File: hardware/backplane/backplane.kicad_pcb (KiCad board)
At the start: 2 copper layers, 200 x 124 mm, 12 parts, among them J1 C96ABC, J2 C96ABC, J3 C96ABC, J4 C96ABC, J5 C96ABC, J6 C96ABC, J7 C96ABC, J8 C96ABC

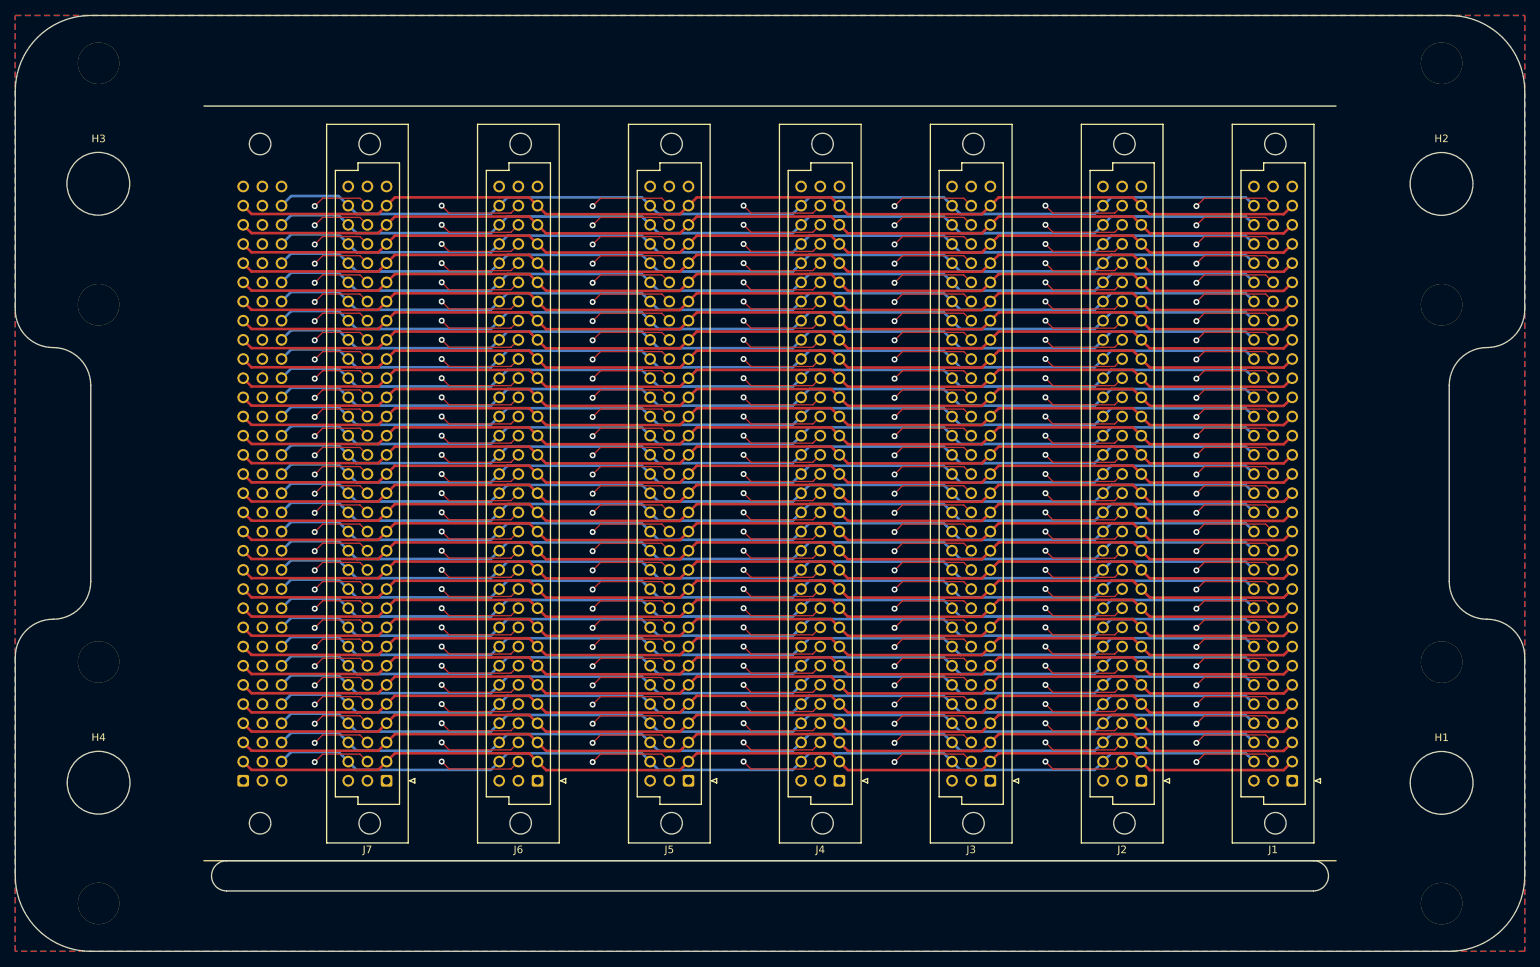
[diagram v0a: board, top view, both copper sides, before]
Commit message: backplane: fix spacing to use 5.08mm HP, expand to 8 back slots with 3/4 spacing
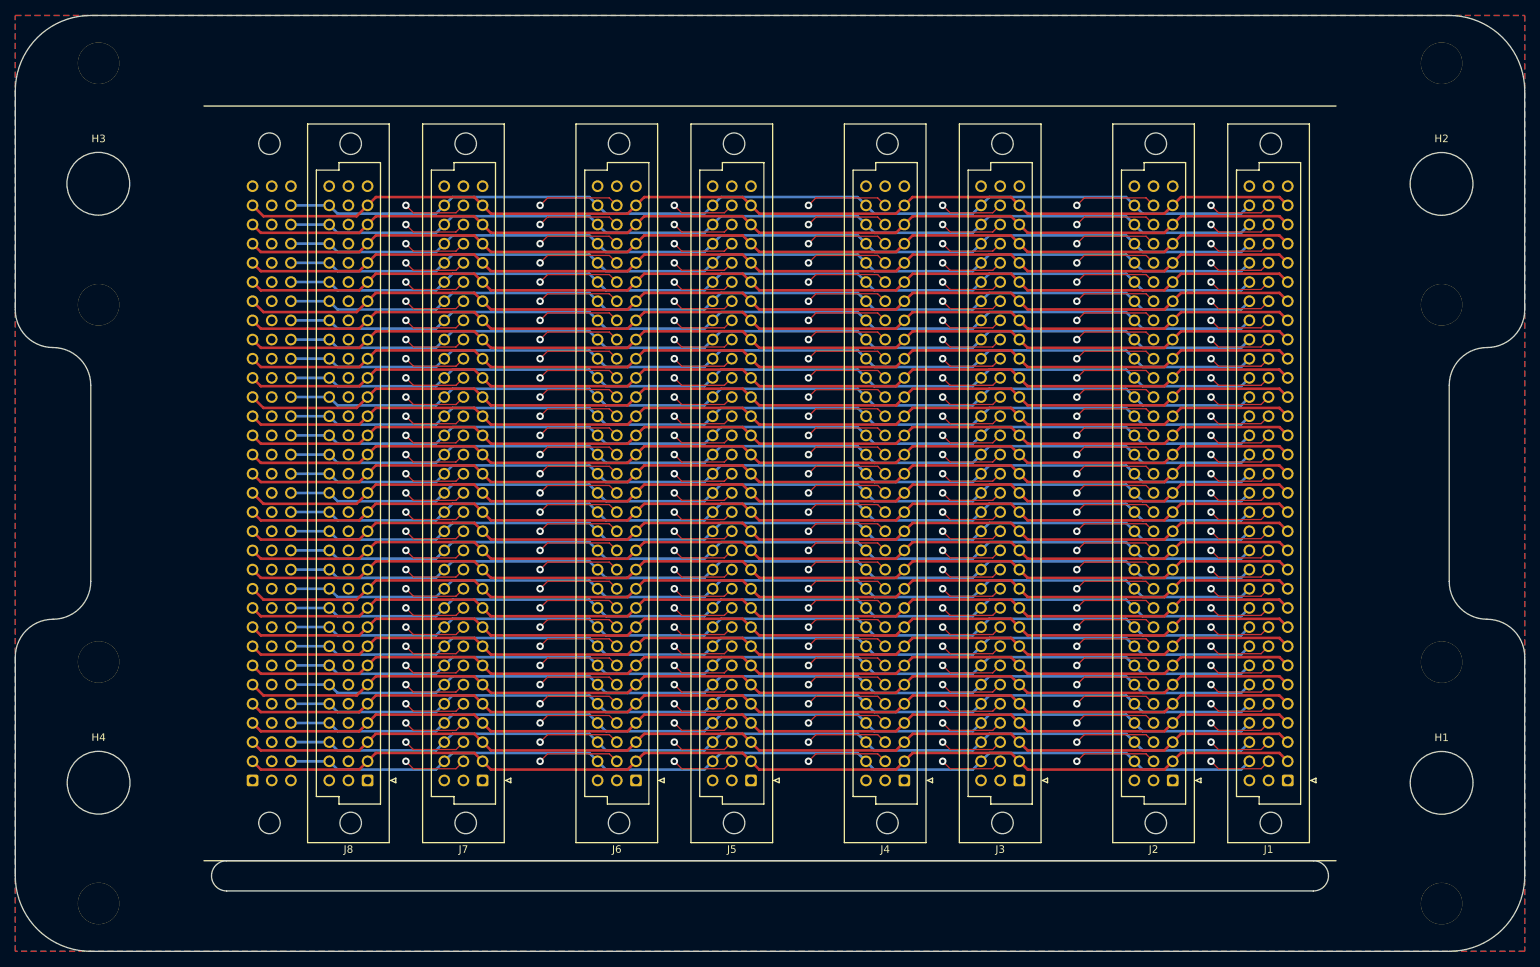
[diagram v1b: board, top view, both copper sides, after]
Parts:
- added J9: C96ABC, Connector_DIN:DIN41612_C_3x32_Female_Vertical_THT, B.Cu at (75.5, 129.9)
- J8: moved to F.Cu
- moved J8 16.5 mm to (90.8, 129.9), turned to 180 degrees
- moved J6 13.0 mm to (126.3, 129.9)
- moved J7 12.7 mm to (106.0, 129.9)
- moved J4 8.60 mm to (161.9, 129.9)
- moved J5 8.28 mm to (141.6, 129.9)
- moved J2 4.16 mm to (197.4, 129.9)
- moved J3 3.84 mm to (177.1, 129.9)
- moved J1 0.60 mm to (212.7, 129.9)
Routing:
- net B2J1: track 11.0 -> 8.44 mm
- net B7J1: track 11.0 -> 8.44 mm
- net B2J5: track 11.0 -> 8.44 mm
- net B28J1: track 11.0 -> 8.44 mm
- net B2J3: track 11.0 -> 8.44 mm
- net B9J1: track 11.0 -> 8.44 mm
- net B8J1: track 11.0 -> 8.44 mm
- net B6J1: track 11.0 -> 8.44 mm
- net B4J1: track 11.0 -> 8.44 mm
- net B29J1: track 11.0 -> 8.44 mm
- net B25J1: track 11.0 -> 8.44 mm
- net B24J1: track 11.0 -> 8.44 mm
- net B22J1: track 11.0 -> 8.44 mm
- net B20J1: track 11.0 -> 8.44 mm
- net B18J1: track 11.0 -> 8.44 mm
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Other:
- net class B: via_dia 1.5 -> 1; via_drill 0.6 -> 0.5

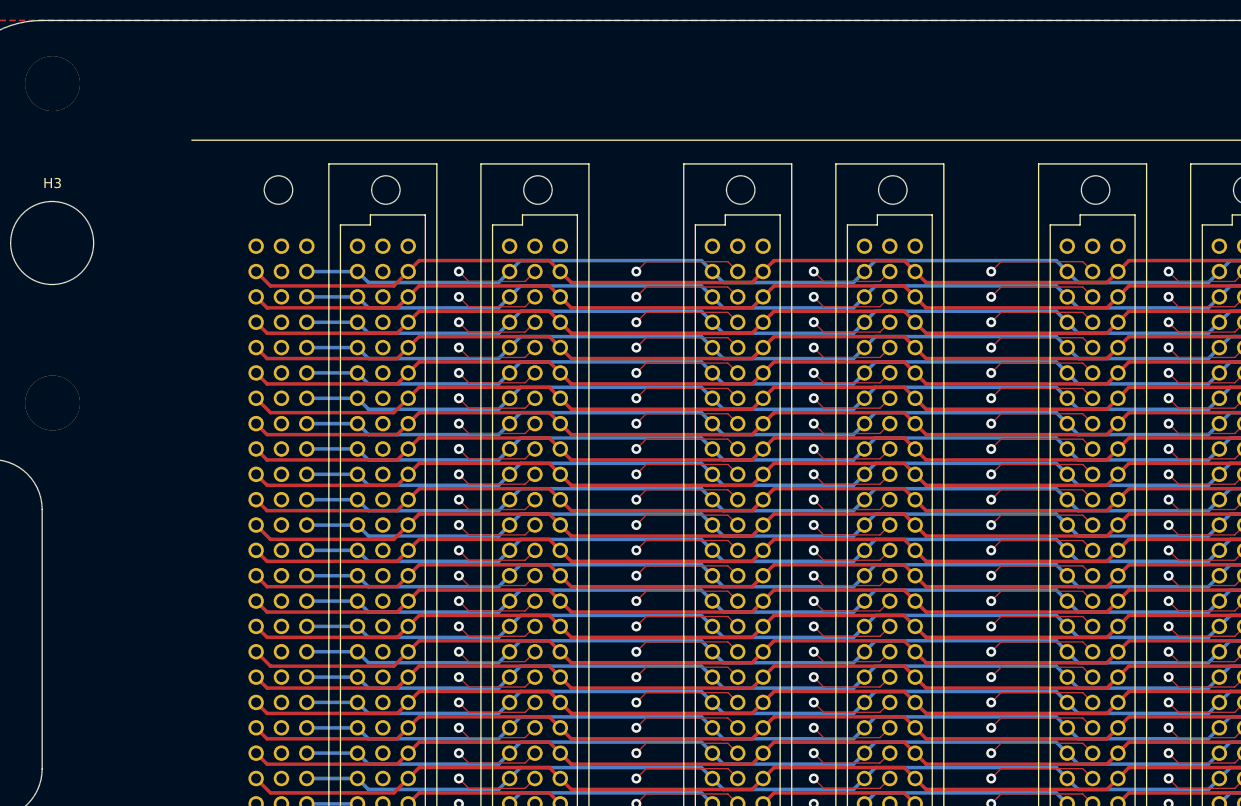
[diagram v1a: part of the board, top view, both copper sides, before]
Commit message: start to put clock hardware on the backplane
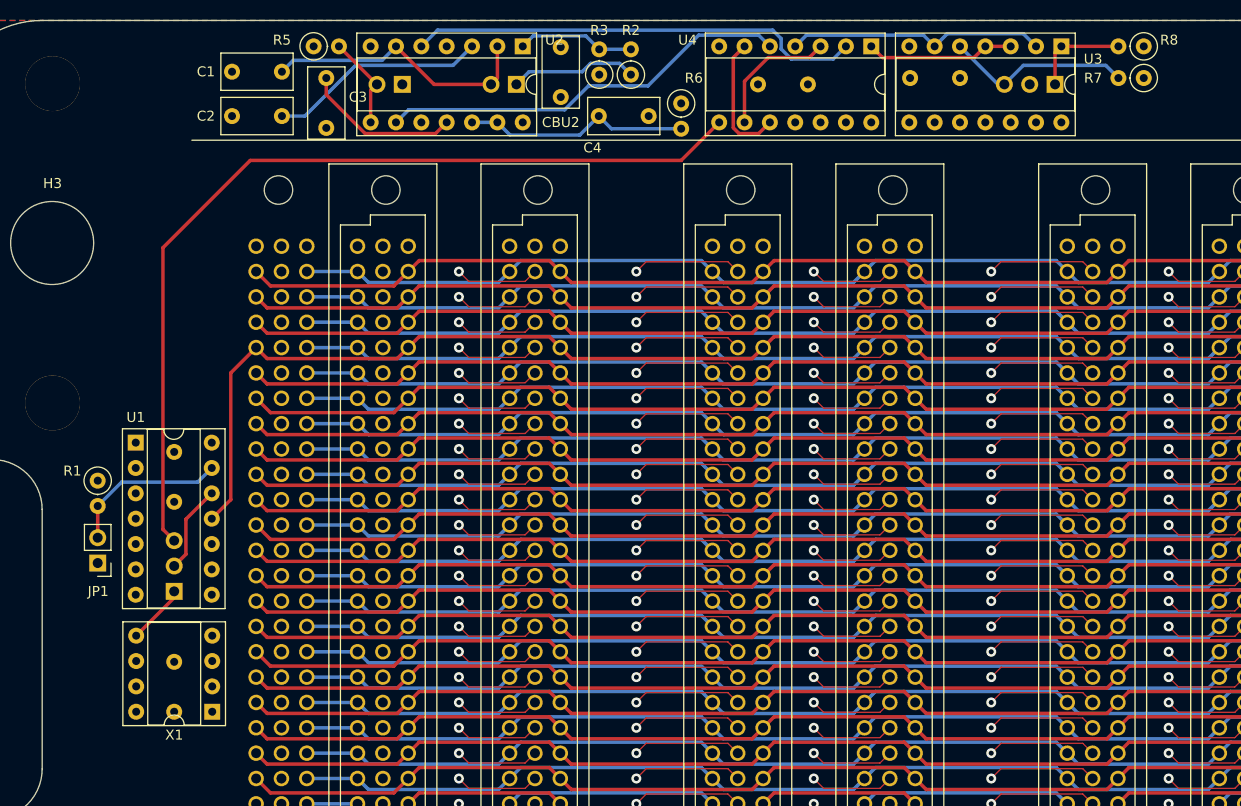
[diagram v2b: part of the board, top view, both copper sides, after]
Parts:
- added C1: 1μF, Capacitor_THT:C_Rect_L7.0mm_W3.5mm_P5.00mm, F.Cu at (78.1, 33.7)
- added C2: 0.01μF, Capacitor_THT:C_Rect_L7.0mm_W3.5mm_P5.00mm, F.Cu at (78.1, 38.1)
- added C3: 0.01μF, Capacitor_THT:C_Rect_L7.0mm_W3.5mm_P5.00mm, F.Cu at (82.5, 34.3)
- added C4: 1μF, Capacitor_THT:C_Rect_L7.0mm_W3.5mm_P5.00mm, F.Cu at (109.9, 38.1)
- added CBU1: 0.1μF, Capacitor_THT:C_Rect_L7.0mm_W3.5mm_P5.00mm, B.Cu at (67.3, 71.8)
- added CBU2: 0.1μF, Capacitor_THT:C_Rect_L7.0mm_W3.5mm_P5.00mm, F.Cu at (106.0, 36.2)
- added CBU3: 0.1μF, Capacitor_THT:C_Rect_L7.0mm_W3.5mm_P5.00mm, B.Cu at (146.1, 34.3)
- added CBU4: 0.1μF, Capacitor_THT:C_Rect_L7.0mm_W3.5mm_P5.00mm, B.Cu at (130.8, 34.9)
- added CBX1: 0.1μF, Capacitor_THT:C_Rect_L7.0mm_W3.5mm_P5.00mm, B.Cu at (67.3, 97.8)
- added JP1: Jumper_NO_Small, Connector_PinHeader_2.54mm:PinHeader_1x02_P2.54mm_Vertical, F.Cu at (59.6, 82.9)
- added R1: 4.7k, Resistor_THT:R_Axial_DIN0207_L6.3mm_D2.5mm_P2.54mm_Vertical, F.Cu at (59.6, 74.6)
- added R2: 1k, Resistor_THT:R_Axial_DIN0207_L6.3mm_D2.5mm_P2.54mm_Vertical, F.Cu at (113.1, 34.0)
- added R3: 1k, Resistor_THT:R_Axial_DIN0207_L6.3mm_D2.5mm_P2.54mm_Vertical, F.Cu at (109.9, 34.0)
- added R4: 100k, Connector_PinHeader_2.54mm:PinHeader_1x02_P2.54mm_Vertical, B.Cu at (101.6, 34.9)
- added R5: 1k, Resistor_THT:R_Axial_DIN0207_L6.3mm_D2.5mm_P2.54mm_Vertical, F.Cu at (81.3, 31.1)
- added R6: 1k, Resistor_THT:R_Axial_DIN0207_L6.3mm_D2.5mm_P2.54mm_Vertical, F.Cu at (118.1, 36.8)
- added R7: 1k, Resistor_THT:R_Axial_DIN0207_L6.3mm_D2.5mm_P2.54mm_Vertical, F.Cu at (164.5, 34.3)
- added R8: 1k, Resistor_THT:R_Axial_DIN0207_L6.3mm_D2.5mm_P2.54mm_Vertical, F.Cu at (164.5, 31.1)
- added SW1: SW_SPDT, Connector_PinHeader_2.54mm:PinHeader_1x03_P2.54mm_Vertical, B.Cu at (67.3, 85.7)
- added SW2: SW_Push, Connector_PinHeader_2.54mm:PinHeader_1x02_P2.54mm_Vertical, B.Cu at (90.2, 34.9)
- added SW3: SW_SPDT, Connector_PinHeader_2.54mm:PinHeader_1x03_P2.54mm_Vertical, B.Cu at (155.6, 34.9)
- added U1: 74AHCT125, Package_DIP:DIP-14_W7.62mm_Socket, F.Cu at (63.5, 70.8)
- added U2: NE556, Package_DIP:DIP-14_W7.62mm_Socket, F.Cu at (102.2, 31.1)
- added U3: 74HC00, Package_DIP:DIP-14_W7.62mm_Socket, F.Cu at (156.2, 31.1)
- added U4: 74HC00, Package_DIP:DIP-14_W7.62mm_Socket, F.Cu at (137.2, 31.1)
- added X1: CXO_DIP8, Package_DIP:DIP-8_W7.62mm_Socket, F.Cu at (71.1, 97.8)
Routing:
- net 555_CLK: track 0.00 -> 90.8 mm
- net 555_AST: track 0.00 -> 45.5 mm
- net 555_MONO: track 0.00 -> 41.6 mm
- net Net-(C1-Pad1): track 0.00 -> 27.7 mm
- net SEL_MONO: track 0.00 -> 26.1 mm
- net Net-(C4-Pad1): track 0.00 -> 22.8 mm
- net Net-(C2-Pad1): track 0.00 -> 21.9 mm
- net A28: track 144.5 -> 163.4 mm
- net Net-(R7-Pad2): track 0.00 -> 18.8 mm
- net ~CLK_ENABLE~: track 0.00 -> 16.2 mm
- net Net-(C3-Pad1): track 0.00 -> 15.8 mm
- net SEL_AST: track 0.00 -> 14.9 mm
- net Net-(U4-Pad3): track 0.00 -> 13.2 mm
- net Net-(U4-Pad10): track 0.00 -> 13.0 mm
- net Net-(R2-Pad1): track 0.00 -> 12.8 mm
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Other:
- board text added: "Clock adjust"
- board text added: "Step"
- board text added: "astable/mono toggle"
